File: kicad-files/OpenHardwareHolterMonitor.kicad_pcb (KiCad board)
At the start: 8 copper layers, 165 x 130 mm, 147 parts, among them CON1 Micro_SD_Card, J1 Conn_02x06_Odd_Even, J10 Conn_01x01, J11 Conn_01x01, J12 USB_OTG, J13 USB_C_Receptacle, J2 Conn_01x01, J3 Conn_01x01, J4 Conn_01x01, J5 Conn_01x01, J6 Conn_01x01, J7 Conn_01x01, J8 Conn_01x01, J9 Conn_01x01, P1 Custom_FTDI, Q1 S8050, Q10 Q_PMOS_DGS, Q2 S8050, Q3 Q_NMOS_DGS, Q4 Q_NMOS_DGS, Q5 Q_NMOS_DGS, Q6 Q_NMOS_DGS, Q7 Q_PMOS_DGS, Q8 Q_PMOS_DGS, Q9 Q_PMOS_DGS, SW1 SW_SPDT, U1 ESP-WROOM-32, U2 ADS1298, U3 MCP73833, U4 MCP73833, U5 TPS2113A, U6 LP5912, U7 REM_3-xxxxS, Y1 32768Hz

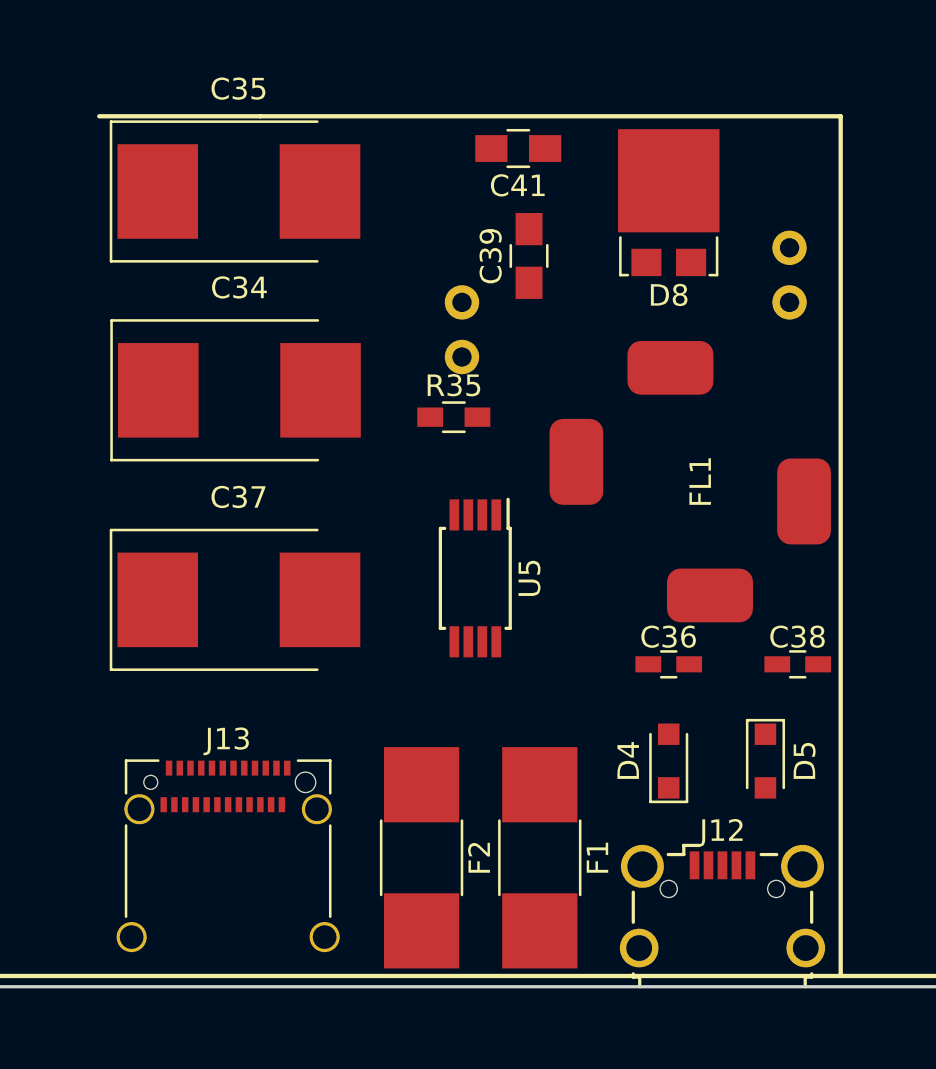
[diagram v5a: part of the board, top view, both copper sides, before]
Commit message: non-isolated hook-up
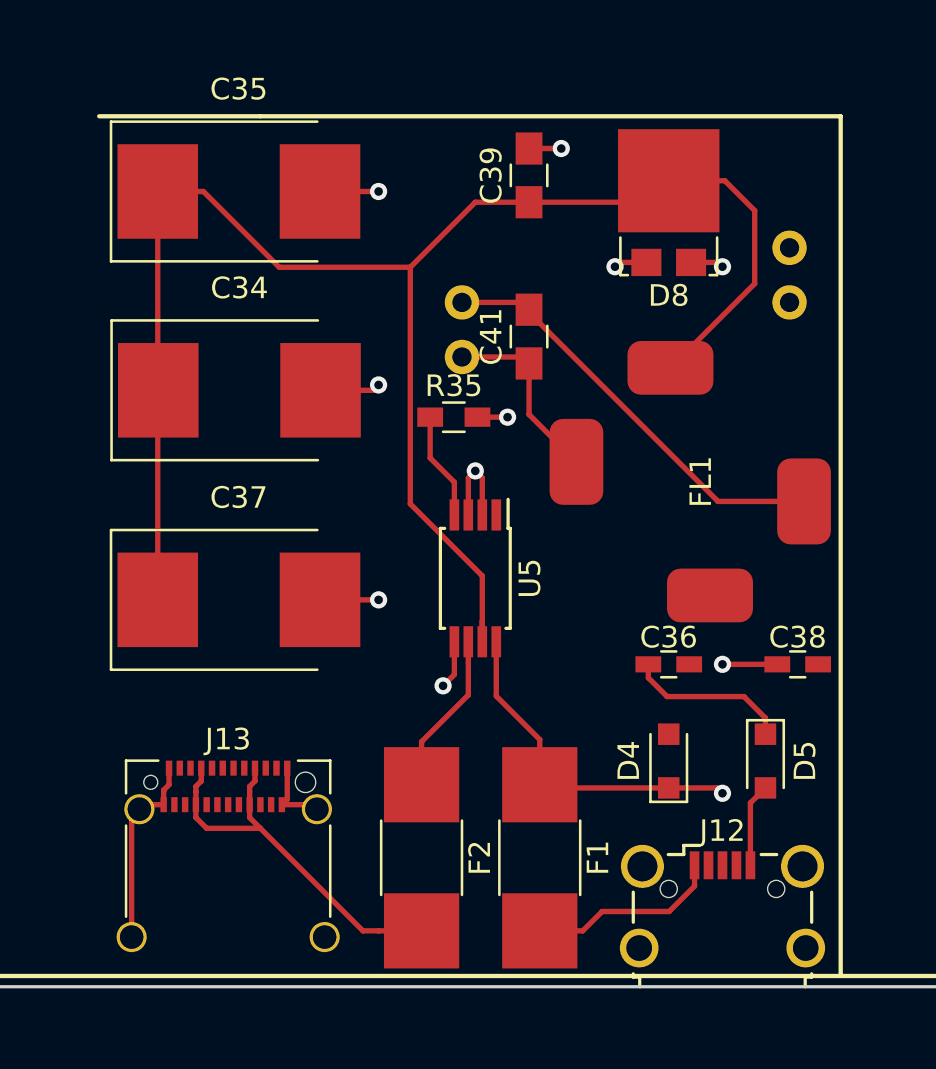
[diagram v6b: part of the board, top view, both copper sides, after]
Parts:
- moved C41 8.76 mm to (159.5, 69.8), turned to 90 degrees
- moved C39 3.75 mm to (159.5, 62.2)
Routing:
- net /power/MUX_POWER_OUT: track 0.00 -> 79.2 mm
- net GNDPWR: track 0.00 -> 37.4 mm, vias 0 -> 9
- net Net-(C41-Pad1): track 0.00 -> 28.0 mm
- net /power/USB_MICRO_IN: track 0.00 -> 24.7 mm, vias 0 -> 2
- net Net-(C41-Pad2): track 0.00 -> 19.8 mm
- net +5C: track 0.00 -> 18.2 mm
- net /power/USB_C_IN: track 0.00 -> 15.2 mm
- net +5V: track 0.00 -> 9.03 mm
- net Net-(R35-Pad1): track 0.00 -> 5.02 mm

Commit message: pre-notch checkpoint
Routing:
- removed copper zone on In2.Cu.pwr, net +3V3
- removed copper zone on In1.Cu.gnd, net GND
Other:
- board size 165 x 130 mm -> 145 x 80 mm
- board text removed: "Note: will notch the board for the antenna"
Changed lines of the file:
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@@
   (general
     (thickness 1.6)
-    (drawings 16)
+    (drawings 14)
     (tracks 1235)
     (zones 0)
@@
   (gr_line (start 182 99.5) (end 182 52.5) (layer F.SilkS) (width 0.2))
   (gr_line (start 124.5 105) (end 125 105) (layer F.SilkS) (width 0.2))
-  (gr_line (start 105 67.5) (end 105 150) (layer Edge.Cuts) (width 0.15))
-  (gr_line (start 270 20) (end 125 20) (layer Edge.Cuts) (width 0.15))
+  (gr_line (start 270 20) (end 147 20) (layer Edge.Cuts) (width 0.15))
   (gr_line (start 270 100) (end 125 100) (layer Edge.Cuts) (width 0.15))
   (gr_line (start 270 20) (end 270 100) (layer Edge.Cuts) (width 0.15))
@@
   (gr_line (start 269.5 99.5) (end 51.8 99.5) (layer F.SilkS) (width 0.2))
   (gr_line (start 269.5 99.5) (end 269.5 20.5) (layer F.SilkS) (width 0.2))
-  (gr_text "Note: will notch the board for the antenna" (at 159.5 18.5) (layer F.Cu)
-    (effects (font (size 1.5 1.5) (thickness 0.3)))
-  )
   (via (at 214 47.5) (size 0.8) (drill 0.4) (layers F.Cu B.Cu) (net 1))
   (segment (start 214 49.95) (end 214 47.5) (width 0.25) (layer F.Cu) (net 1))
@@
   (segment (start 196 81) (end 194.2 81) (width 0.25) (layer F.Cu) (net 143))
   (segment (start 197 80) (end 196 81) (width 0.25) (layer F.Cu) (net 143))
-  (zone (net 1) (net_name GND) (layer In1.Cu.gnd) (hatch edge 0.508)
-    (connect_pads (clearance 0.508))
-    (min_thickness 0.254)
-    (fill yes (arc_segments 16) (thermal_gap 0.508) (thermal_bridge_width 0.508))
-    (polygon
-      (pts
-        (xy 61.25 20.5) (xy 151.5 20.5) (xy 151.5 27.3) (xy 172.5 27.25) (xy 172.5 20.5)
-        (xy 269.35 20.5) (xy 269.35 102.05) (xy 52 102.05)
-      )
-    )
-  )
-  (zone (net 6) (net_name +3V3) (layer In2.Cu.pwr) (hatch edge 0.508)
-    (connect_pads (clearance 0.508))
-    (min_thickness 0.254)
-    (fill yes (arc_segments 16) (thermal_gap 0.508) (thermal_bridge_width 0.508))
-    (polygon
-      (pts
-        (xy 61.25 20.5) (xy 151.5 20.5) (xy 151.5 27.3) (xy 172.5 27.25) (xy 172.5 20.5)
-        (xy 269.35 20.5) (xy 269.35 102.05) (xy 52 102.05)
-      )
-    )
-  )
 )

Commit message: ready for holes and zones
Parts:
- moved C1 8.49 mm to (153.5, 43.0), turned to 180 degrees
- moved J1 3.70 mm to (140.7, 47.2)
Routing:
- net /power/USB_C_IN: track 15.2 -> 24.4 mm, vias 0 -> 2
- net /IO4: track 38.9 -> 43.8 mm
- net /IO13: track 27.4 -> 31.9 mm
- net /IO15: track 35.8 -> 40.2 mm
- net /IO39: track 7.42 -> 11.6 mm
- net /IO36: track 5.62 -> 9.60 mm
- net /IO27: track 19.1 -> 22.4 mm
- net /IO14: track 22.3 -> 25.6 mm
- net /IO2: track 49.1 -> 52.2 mm
- net /IO12: track 28.2 -> 31.1 mm
- net /EN: track 49.2 -> 52.0 mm
- net /RTC_P: track 15.5 -> 12.9 mm
- net /IO0: track 46.6 -> 49.0 mm
- net /RTC_N: track 13.4 -> 14.5 mm
- net /RTS: track 33.1 -> 33.9 mm
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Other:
- board size 145 x 80 mm -> 131 x 80 mm
